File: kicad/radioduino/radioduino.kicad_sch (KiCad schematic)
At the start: 0 parts

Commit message: basic schematic
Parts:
- added A1: Arduino_Nano_v3.x, Module:Arduino_Nano, symbol MCU_Module:Arduino_Nano_v3.x
- added C1, C2, C3: 100n, Capacitor_SMD:C_0805_2012Metric, symbol Device:C
- added C4, C5: 470n, Capacitor_SMD:C_0805_2012Metric, symbol Device:C
- added C6: 10u, Capacitor_SMD:C_0805_2012Metric, symbol Device:C
- added DS1: WC1602A, Display:WC1602A, symbol Display_Character:WC1602A
- added J1: Conn_01x03_Socket, Connector_PinHeader_2.54mm:PinHeader_1x03_P2.54mm_Vertical, symbol Connector:Conn_01x03_Socket
- added J2, J3, J4, J5: Conn_Coaxial_Small, Connector_Coaxial:SMA_Amphenol_132289_EdgeMount, symbol Connector:Conn_Coaxial_Small
- added J6, J7: Conn_01x15, Connector_PinHeader_2.54mm:PinHeader_1x15_P2.54mm_Vertical, symbol Connector_Generic:Conn_01x15
- added JP1, JP2, JP3, JP8: SolderJumper_2_Open, Jumper:SolderJumper-2_P1.3mm_Open_TrianglePad1.0x1.5mm, symbol Jumper:SolderJumper_2_Open
- added JP4, JP6, JP7: SolderJumper_2_Bridged, Jumper:SolderJumper-2_P1.3mm_Bridged_Pad1.0x1.5mm, symbol Jumper:SolderJumper_2_Bridged
- added JP5: SolderJumper_3_Open, Jumper:SolderJumper-3_P1.3mm_Open_Pad1.0x1.5mm, symbol Jumper:SolderJumper_3_Open
- added Q1: SS8050, Package_TO_SOT_SMD:SOT-23, symbol Transistor_BJT:SS8050
- added Q2, Q3: BSS138, Package_TO_SOT_SMD:SOT-23, symbol Transistor_FET:BSS138
- added R1, R10, R11, R12, R2, R3, R7, R8, R9: 10K, Resistor_SMD:R_0805_2012Metric_Pad1.20x1.40mm_HandSolder, symbol Device:R
- added R4, R5, R6: 4.7K, Resistor_SMD:R_0805_2012Metric_Pad1.20x1.40mm_HandSolder, symbol Device:R
- added RV1: R_Potentiometer, Potentiometer_THT:Potentiometer_Runtron_RM-065_Vertical, symbol Device:R_Potentiometer
- added SW1: RotaryEncoder_Switch_MP, Rotary_Encoder:RotaryEncoder_Alps_EC11E-Switch_Vertical_H20mm, symbol Device:RotaryEncoder_Switch_MP
- added U1: PCF8574AT, Package_SO:SOIC-16W_7.5x10.3mm_P1.27mm, symbol Interface_Expansion:PCF8574AT
- added U2: RT9193-33GB, SOT-23-5_RIT, symbol rt9193:RT9193-33GB
- added Y1: Si5351A-B-GT, Package_SO:MSOP-10_3x3mm_P0.5mm, symbol Oscillator:Si5351A-B-GT
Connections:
- new net: J1.2 (Pin_2), JP5.2 (C)
- new net: A1.30 (VIN), J7.15 (Pin_15), JP5.3 (B)
- new net: C3.1, JP7.1 (A)
- new net: C2.2, C3.2, Y1.2 (XA)
- new net: JP2.2 (B), R2.2, U1.2 (A1)
- new net: JP3.2 (B), R3.2, U1.3 (A2)
- new net: A1.10 (D7), J6.10 (Pin_10), R12.1, SW1.B
- new net: Q1.1 (B), R6.2, U1.7 (P3)
- new net: Q3.3 (D), R10.2, Y1.5 (SDA)
- new net: J3.1 (In), Y1.10 (CLK0)
- new net: Q2.3 (D), R9.2, Y1.4 (SCL)
- new net: J5.1 (In), Y1.6 (CLK2)
- new net: J4.1 (In), Y1.9 (CLK1)
- new net: A1.24 (A5), J7.9 (Pin_9), Q2.2 (S), R5.2, R7.2, U1.14 (SCL)
- new net: DS1.3 (VO), RV1.2
- new net: JP1.2 (B), R1.2, U1.1 (A0)
- new net: A1.16 (D13), J7.1 (Pin_1)
- new net: A1.25 (A6), J7.10 (Pin_10)
- new net: A1.26 (A7), J7.11 (Pin_11)
- new net: A1.27 (+5V), J7.12 (Pin_12), JP4.1 (A)
- new net: A1.28 (~{RESET}), J7.13 (Pin_13)
- new net: A1.18 (AREF), J7.3 (Pin_3)
- new net: A1.19 (A0), J7.4 (Pin_4)
- new net: A1.20 (A1), J7.5 (Pin_5)
- new net: A1.21 (A2), J7.6 (Pin_6)
- new net: A1.22 (A3), J7.7 (Pin_7)
- new net: A1.23 (A4), J7.8 (Pin_8), Q3.2 (S), R4.2, R8.1, U1.15 (SDA)
- new net: A1.9 (D6), J6.9 (Pin_9), R11.1, SW1.A
- new net: A1.1 (D1/TX), J6.1 (Pin_1)
- new net: A1.11 (D8), J6.11 (Pin_11), SW1.S1
- new net: A1.12 (D9), J6.12 (Pin_12)
- new net: A1.13 (D10), J6.13 (Pin_13)
- new net: A1.14 (D11), J6.14 (Pin_14)
- new net: A1.15 (D12), J6.15 (Pin_15)
- new net: A1.2 (D0/RX), J6.2 (Pin_2)
- new net: A1.3 (~{RESET}), J6.3 (Pin_3)
- new net: A1.5 (D2), J6.5 (Pin_5)
- new net: A1.6 (D3), J6.6 (Pin_6)
- new net: A1.7 (D4), J6.7 (Pin_7)
- new net: A1.8 (D5), J6.8 (Pin_8)
- new net: DS1.15 (LED(+)), JP6.2 (B)
- new net: DS1.12 (D5), U1.10 (P5)
- new net: DS1.13 (D6), U1.11 (P6)
- new net: DS1.14 (D7), U1.12 (P7)
- new net: DS1.4 (RS), U1.4 (P0)
- new net: DS1.5 (R/W), U1.5 (P1)
- new net: DS1.6 (E), U1.6 (P2)
- new net: DS1.11 (D4), U1.9 (P4)
- new net: J2.1 (In), JP8.1 (A)
- new net: C2.1, JP8.2 (B)
- new net: DS1.16 (LED(-)), Q1.3 (C)
- new net +3.3V: C4.2, C5.1, Q2.1 (G), Q3.1 (G), R10.1, R9.1, U2.5 (VOUT), Y1.1 (VDD), Y1.7 (VDDO)
- new net +5V: C1.1, C6.1, DS1.2 (VDD), JP4.2 (B), JP5.1 (A), JP6.1 (A), R1.1, R11.2, R12.2, R2.1, R3.1, R4.1, R5.1, R6.1, R7.1, R8.2, RV1.1, U2.1 (VIN), U2.3 (EN)
- new net GND: A1.29 (GND), A1.4 (GND), C1.2, C4.1, C5.2, C6.2, DS1.1 (VSS), J1.1 (Pin_1), J1.3 (Pin_3), J2.2 (Ext), J3.2 (Ext), J4.2 (Ext), J5.2 (Ext), J6.4 (Pin_4), J7.14 (Pin_14), J7.2 (Pin_2), JP1.1 (A), JP2.1 (A), JP3.1 (A), Q1.2 (E), RV1.3, SW1.C, SW1.S2, U2.2 (GND)
- no-connect marks 0 -> 1
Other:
- company: (none) -> YO3DBZ
- title: (none) -> Radioduino

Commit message: made pcb
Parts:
- added U3: (no value), Crystal:Crystal_SMD_2016-4Pin_2.0x1.6mm, symbol radioduino:1XXD32000MBA
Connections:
- net +3.3V: now also U3.4 (VCC)
- net GND: now also Y1.3 (XB), U3.1 (GND), U3.2 (GND); no longer J7.14 (Pin_14)
- net vin: now reaches A1.30 (VIN), JP5.3 (B)
- net vin: now also J7.1 (Pin_1); no longer J7.15 (Pin_15)
- net d7: now reaches A1.10 (D7), J6.10 (Pin_10), R12.1, SW1.B
- net at JP7.2 (B): now also U3.3 (OUT)
- net scl: now reaches A1.24 (A5), Q2.2 (S), R5.2, R7.2, U1.14 (SCL)
- net scl: now also J7.7 (Pin_7); no longer J7.9 (Pin_9)
- net d13: now reaches A1.16 (D13)
- net d13: now also J7.15 (Pin_15); no longer J7.1 (Pin_1)
- net a2: now reaches J7.10 (Pin_10)
- net a2: now also A1.21 (A2); no longer A1.25 (A6)
- net a1: now reaches J7.11 (Pin_11)
- net a1: now also A1.20 (A1); no longer A1.26 (A7)
- net 5va: now reaches A1.27 (+5V), JP4.1 (A)
- net 5va: now also J7.4 (Pin_4); no longer J7.12 (Pin_12)
- net aref: now reaches J7.13 (Pin_13)
- net aref: now also A1.18 (AREF); no longer A1.28 (~{RESET})
- net rst2: now reaches J7.3 (Pin_3)
- net rst2: now also A1.28 (~{RESET}); no longer A1.18 (AREF)
- net a0: now reaches A1.19 (A0)
- net a0: now also J7.12 (Pin_12); no longer J7.4 (Pin_4)
- net a7: now reaches J7.5 (Pin_5)
- net a7: now also A1.26 (A7); no longer A1.20 (A1)
- net a6: now reaches J7.6 (Pin_6)
- net a6: now also A1.25 (A6); no longer A1.21 (A2)
- net a3: now reaches A1.22 (A3)
- net a3: now also J7.9 (Pin_9); no longer J7.7 (Pin_7)
- net sda: now reaches A1.23 (A4), J7.8 (Pin_8), Q3.2 (S), R4.2, R8.1, U1.15 (SDA)
- net d6: now reaches A1.9 (D6), J6.9 (Pin_9), R11.1, SW1.A
- net tx: now reaches A1.1 (D1/TX), J6.1 (Pin_1)
- net d8: now reaches A1.11 (D8), J6.11 (Pin_11), SW1.S1
- net d9: now reaches A1.12 (D9), J6.12 (Pin_12)
- net d10: now reaches A1.13 (D10), J6.13 (Pin_13)
- net d11: now reaches A1.14 (D11), J6.14 (Pin_14)
- net d12: now reaches A1.15 (D12), J6.15 (Pin_15)
- net rx: now reaches A1.2 (D0/RX), J6.2 (Pin_2)
- net rst1: now reaches A1.3 (~{RESET}), J6.3 (Pin_3)
- net d2: now reaches A1.5 (D2), J6.5 (Pin_5)
- net d3: now reaches A1.6 (D3), J6.6 (Pin_6)
- net d4: now reaches A1.7 (D4), J6.7 (Pin_7)
- net d5: now reaches A1.8 (D5), J6.8 (Pin_8)
- net 3.3A: now reaches A1.17 (3V3)
- net 3.3A: now also J7.14 (Pin_14)
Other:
- moved on the sheet: A1, C1, C2, C3, C4, C5, C6, DS1, J1, J2, J3, J4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

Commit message: pcb
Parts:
- added C7, C8, C9: 100n, Capacitor_SMD:C_0805_2012Metric, symbol Device:C
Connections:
- net at Y1.10 (CLK0): now also C7.1; no longer J3.1 (In)
- net at Y1.6 (CLK2): now also C9.1; no longer J5.1 (In)
- net at Y1.9 (CLK1): now also C8.1; no longer J4.1 (In)
- new net: C9.2, J5.1 (In)
- new net: C8.2, J4.1 (In)
- new net: C7.2, J3.1 (In)
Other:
- moved on the sheet: J3, J4, J5

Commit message: before ldo
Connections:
- net GND: now also Y1.8 (GND)
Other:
- moved on the sheet: C2, C3, C4, C5, C7, C8, C9, J2, J3, J4, J5, JP7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

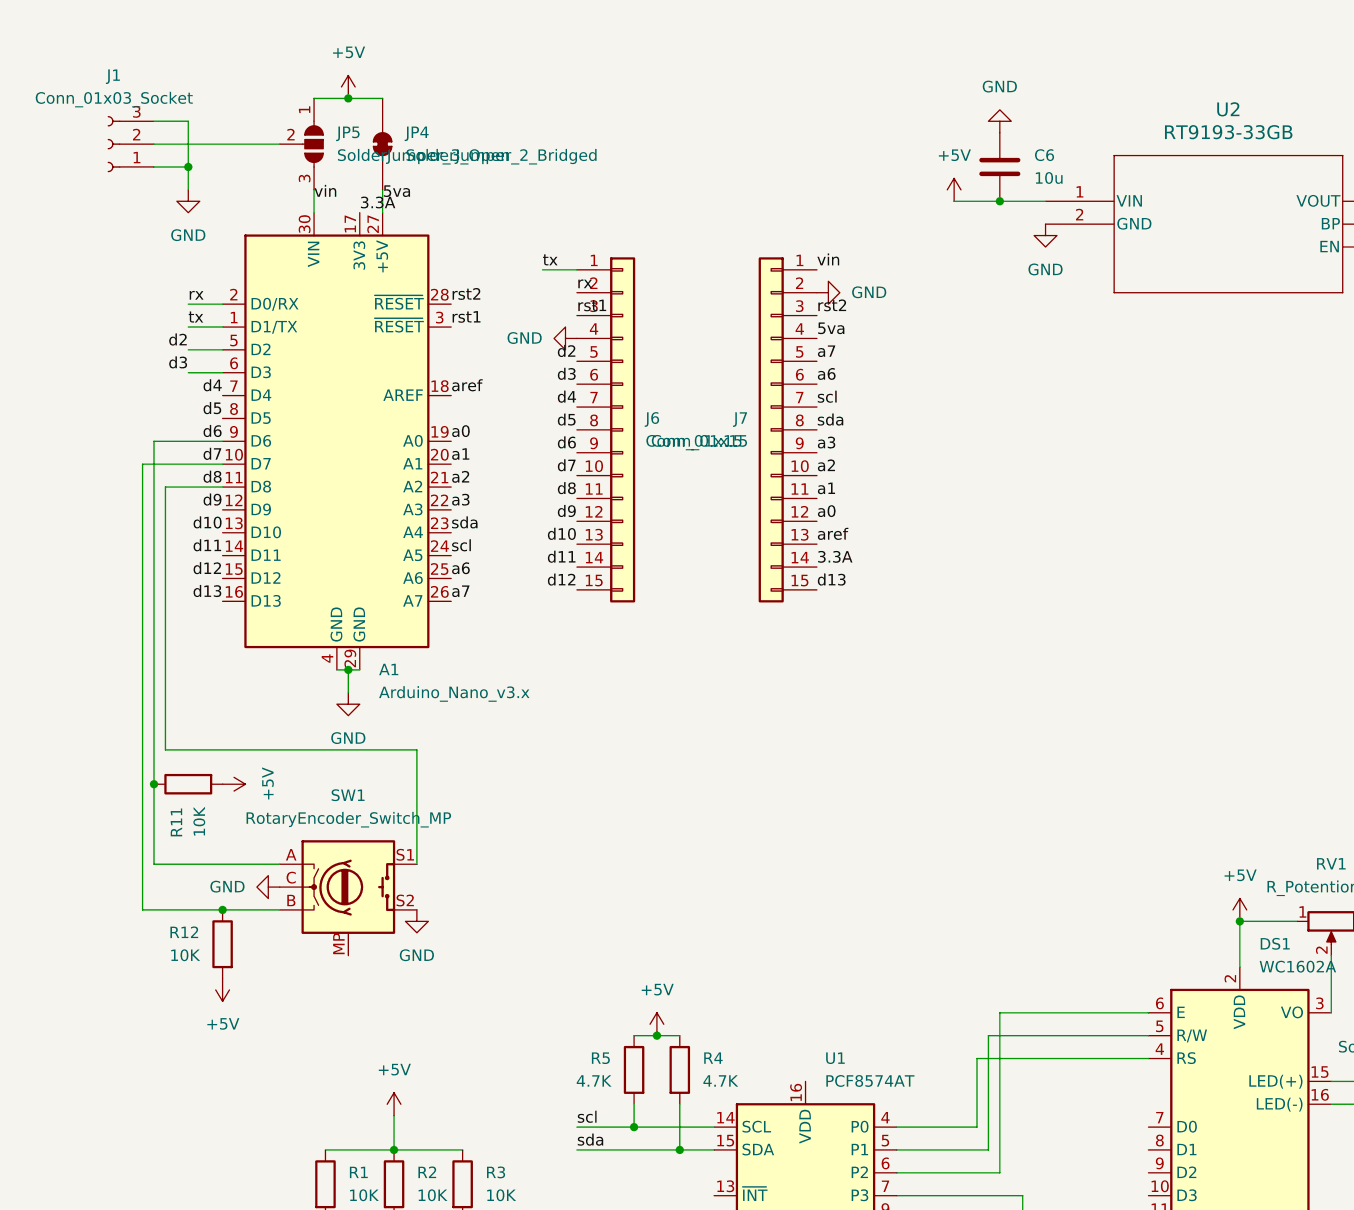
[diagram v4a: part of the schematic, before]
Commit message: 
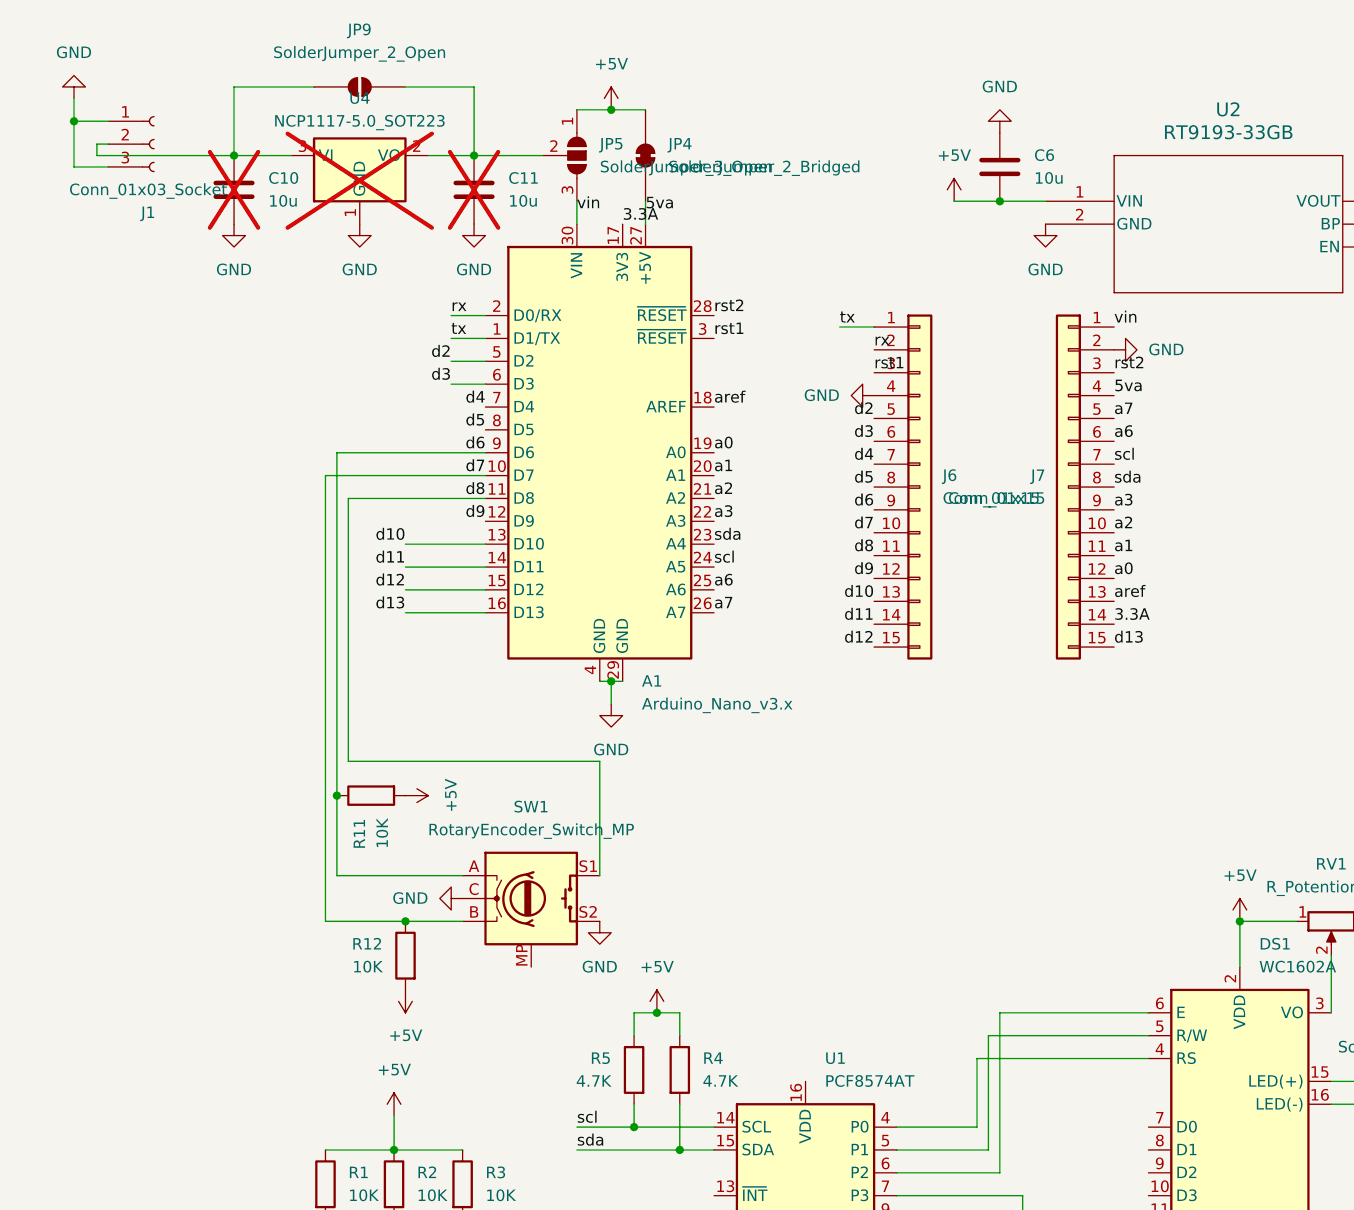
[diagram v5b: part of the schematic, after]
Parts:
- added C10, C11: 10u, Capacitor_SMD:C_0805_2012Metric, symbol Device:C
- added JP9: SolderJumper_2_Open, Jumper:SolderJumper-2_P1.3mm_Open_TrianglePad1.0x1.5mm, symbol Jumper:SolderJumper_2_Open
- added U4: NCP1117-5.0_SOT223, Package_TO_SOT_SMD:SOT-223-3_TabPin2, symbol Regulator_Linear:NCP1117-5.0_SOT223
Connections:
- net GND: now also C10.1, C11.1, U4.1 (GND)
- net at JP5.2 (C): now also C11.2, JP9.2 (B), U4.2 (VO); no longer J1.2 (Pin_2)
- new net: C10.2, J1.2 (Pin_2), JP9.1 (A), U4.3 (VI)
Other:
- moved on the sheet: A1, J1, J6, J7, JP4, JP5, R11, R12, SW1

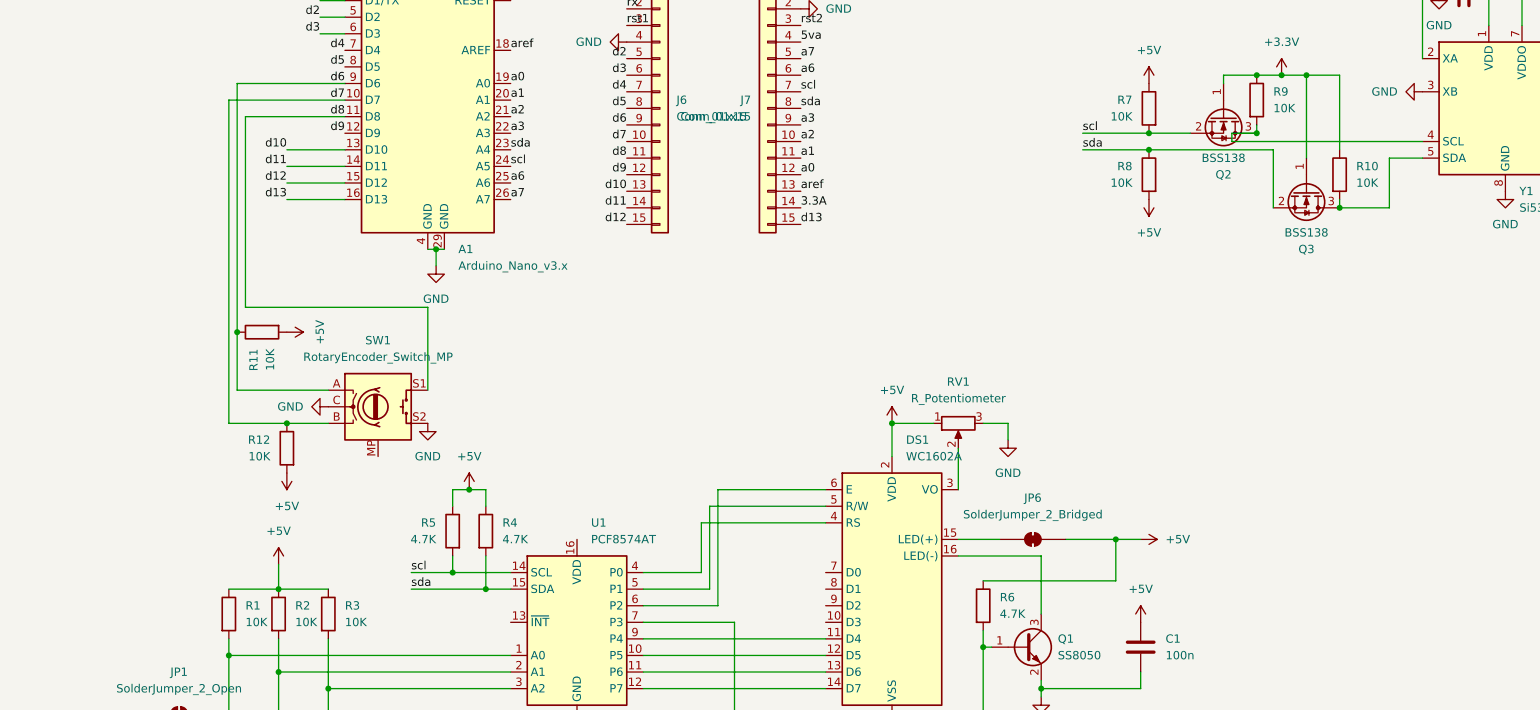
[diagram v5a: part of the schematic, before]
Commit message: fixed pcb added encoder for rit
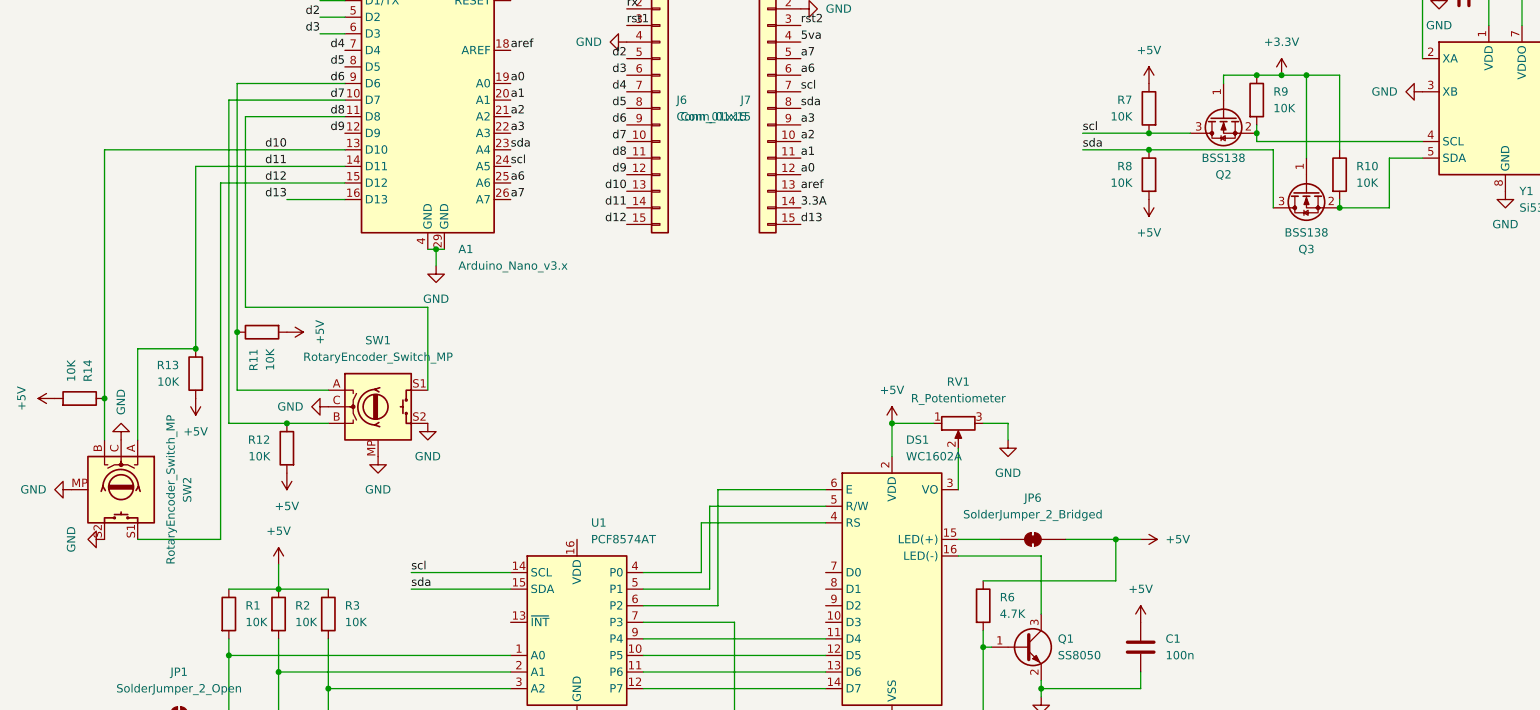
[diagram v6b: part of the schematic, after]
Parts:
- removed R4, R5: 4.7K, Resistor_SMD:R_0805_2012Metric_Pad1.20x1.40mm_HandSolder, symbol Device:R
- added R13, R14: 10K, Resistor_SMD:R_0805_2012Metric_Pad1.20x1.40mm_HandSolder, symbol Device:R
- added SW2: RotaryEncoder_Switch_MP, Rotary_Encoder:RotaryEncoder_Alps_EC11E-Switch_Vertical_H20mm, symbol Device:RotaryEncoder_Switch_MP
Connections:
- net +5V: now also R13.2, R14.2
- net GND: now also SW1.MP, SW2.C, SW2.MP, SW2.S2
- net d10: now also R14.1, SW2.B
- net d11: now also R13.1, SW2.A
- net d12: now also SW2.S1
- net scl: now also Q2.3 (D); no longer Q2.2 (S)
- net sda: now also Q3.3 (D); no longer Q3.2 (S)
- net at R10.2, Y1.5 (SDA): now also Q3.2 (S); no longer Q3.3 (D)
- net at R9.2, Y1.4 (SCL): now also Q2.2 (S); no longer Q2.3 (D)
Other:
- moved on the sheet: Q2, Q3
